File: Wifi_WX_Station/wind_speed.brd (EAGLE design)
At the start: 25.7 x 33.6 mm, 7 parts, among them M1 MRF24WB0MA

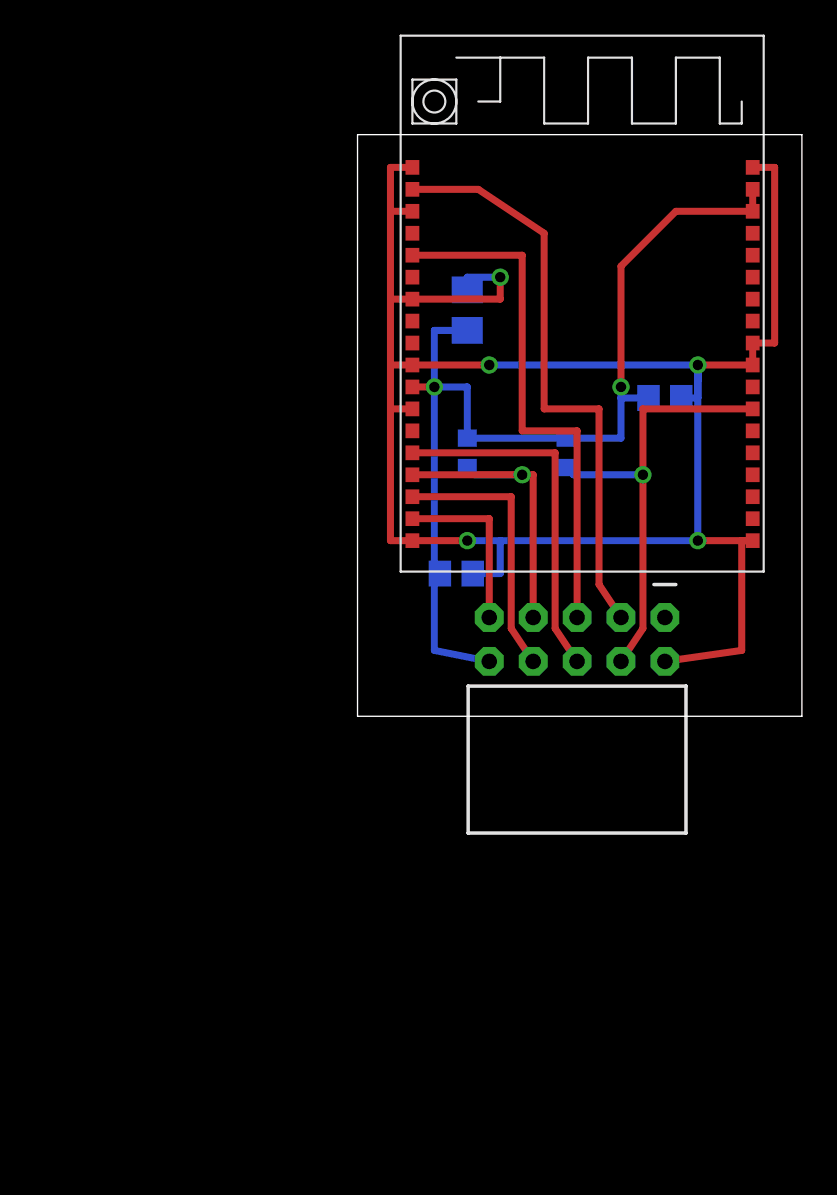
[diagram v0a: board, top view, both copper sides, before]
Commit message: added all the small boards, renamed Wifi module as RH and LH version
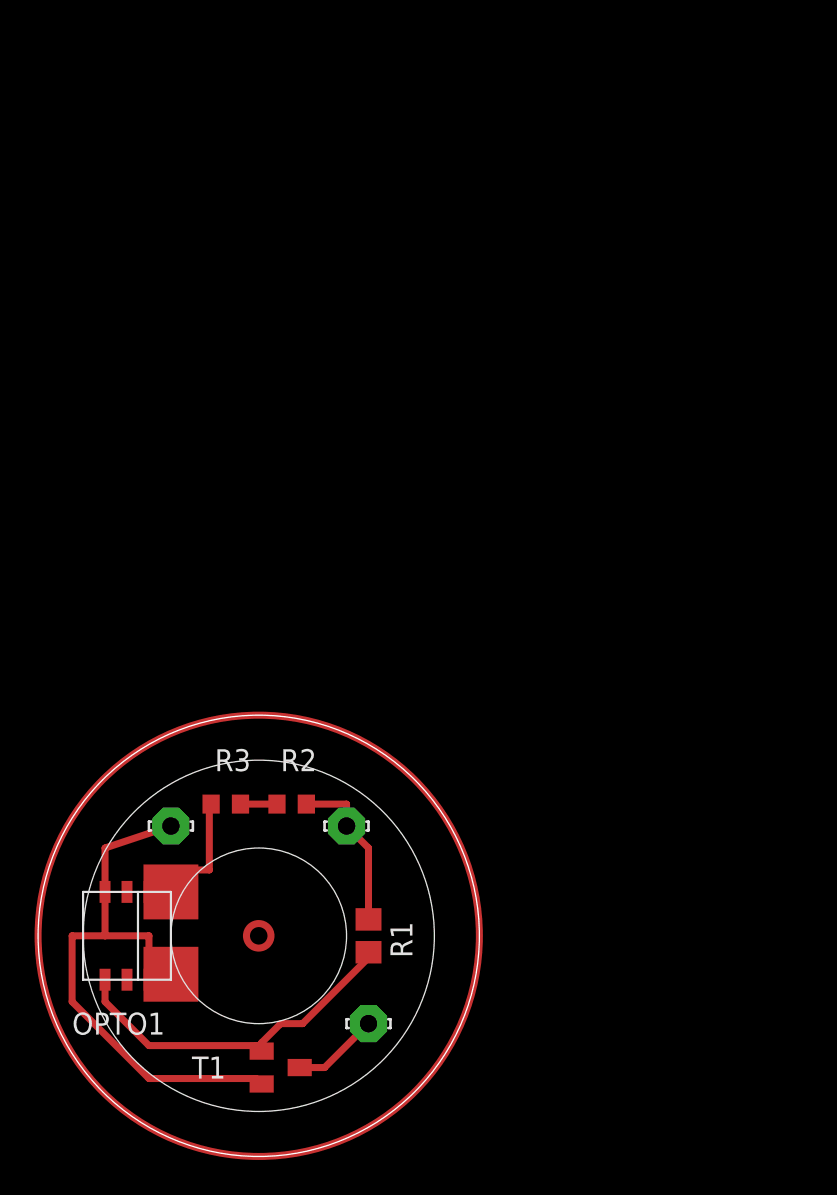
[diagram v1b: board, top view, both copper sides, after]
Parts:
- removed C1, C2: (no value), rcl:C0805
- removed C3: (no value), rcl:R/2012-12R
- removed JP1: M05X2RAF, wifi_WX:2X5-RAF
- removed M1: MRF24WB0MA, 1AA_Stofer:MRF24W
- added +5V, GND, OUT: LSP10, solpad:LSP10
- added OPTO1: OSRAM_SHF9201, 1AA_Stofer:OSRAM-6
- added R3: 120o, rcl:R0603
- added T1: MMBT3904, transistor:SOT23
- R1: value 4.7k -> 10K; device rcl:R0603 -> rcl:R0805
- R2: value 10k -> 120o
- moved R1 28.5 mm to (20.3, 14.0), flipped to the top
- moved R2 25.8 mm to (15.9, 21.6), flipped to the top, turned to 0 degrees
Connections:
- removed net +3V3: C1.1, C2.1, C3.+, JP1.10, M1.16, M1.17, M1.29, R1.2, R2.2
- removed net CS_: JP1.5, M1.23
- removed net GND: C1.2, C2.2, C3.-, JP1.2, M1.1, M1.10, M1.18, M1.19, M1.21, M1.25, M1.28, M1.30, M1.36, M1.9
- removed net HIBER: JP1.3, M1.20
- removed net INT_: JP1.7, M1.33, R1.1
- removed net RESET_: JP1.4, M1.7, R2.1
- removed net SCK: JP1.8, M1.34
- removed net SDI: JP1.9, M1.35
- removed net SDO: JP1.6, M1.32
- new net N$1: OPTO1.P$4, R1.1, T1.1
- new net N$2: GND.MP, OPTO1.P$3, OPTO1.P$6, T1.2
- new net N$3: +5V.MP, R1.2, R2.2
- new net N$4: OUT.MP, T1.3
- new net N$5: OPTO1.P$1, R3.1
- new net N$6: R2.1, R3.2
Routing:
- net GND: track 120.5 -> 0.00 mm, vias 5 -> 0
- net +3V3: track 60.7 -> 0.00 mm, vias 2 -> 0
- net HIBER: track 34.2 -> 0.00 mm
- net N$2: track 0.00 -> 32.8 mm
- net CS_: track 30.5 -> 0.00 mm
- net RESET_: track 26.0 -> 0.00 mm, vias 1 -> 0
- net SDO: track 20.7 -> 0.00 mm
- net N$1: track 0.00 -> 20.5 mm
- net INT_: track 18.6 -> 0.00 mm, vias 1 -> 0
- net SCK: track 15.6 -> 0.00 mm
- net SDI: track 10.2 -> 0.00 mm
- net N$3: track 0.00 -> 9.52 mm
- net N$5: track 0.00 -> 8.67 mm
- net N$4: track 0.00 -> 5.03 mm
- net N$6: track 0.00 -> 2.11 mm
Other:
- board size 25.7 x 33.6 mm -> 25.5 x 25.5 mm
- board text added: "+5V"
- board text added: "GND"
- board text added: "High resolution windspeed encoder"
- board text added: "OUT"
- board text added: "RV-Builders Products 2013"
- board text removed: "0.6000 mm / 23.622 mil"
- board text removed: "0.9000 mm / 35.433 mil"
- board text removed: "1"
- board text removed: "10"
- board text removed: "Date: 12/12/2012 2:51:15 PM"
- board text removed: "Drill legend"
- board text removed: "RV Builders Product 2012"
- board text removed: "Wifi WX-Station"

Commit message: updated BOM with all prices- As Checked in to BATCH PCB
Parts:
- +5V, GND, OUT: value LSP10 -> TPSOL; device solpad:LSP10 -> wifi_WX:TP_SOL
- OPTO1: device 1AA_Stofer:OSRAM-6 -> wifi_WX:OSRAM-6
- R1: device rcl:R0805 -> rcl:R0603
- moved OUT 3.00 mm to (18.7, 6.35)
- moved GND 1.91 mm to (6.99, 20.3)
- moved +5V 1.27 mm to (20.3, 20.3)
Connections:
- net N$2: now also GND.P$1; no longer GND.MP
- net N$3: now also +5V.P$1; no longer +5V.MP
- net N$4: now also OUT.P$1; no longer OUT.MP
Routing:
- net N$4: track 5.03 -> 2.39 mm
- net N$1: track 20.5 -> 22.9 mm
- net N$2: track 32.8 -> 30.6 mm
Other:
- board text added: "High res windspeed encoder"
- board text removed: "High resolution windspeed encoder"

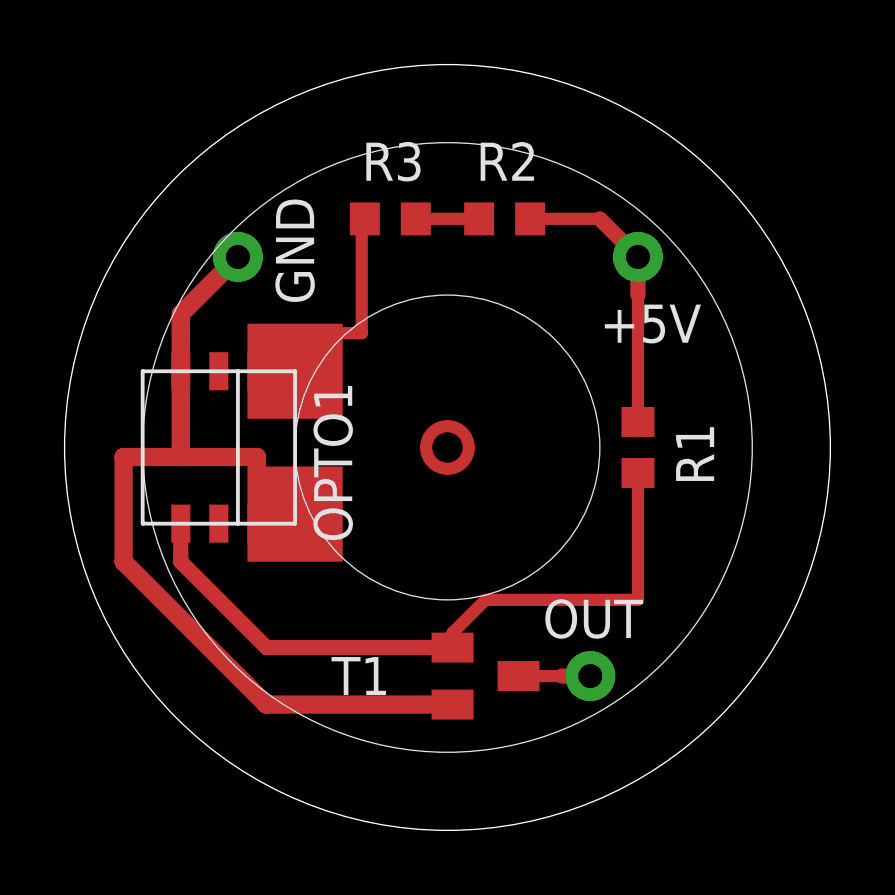
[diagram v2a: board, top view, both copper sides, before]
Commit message: Wind speed board and base station rework to rev HW 1.2
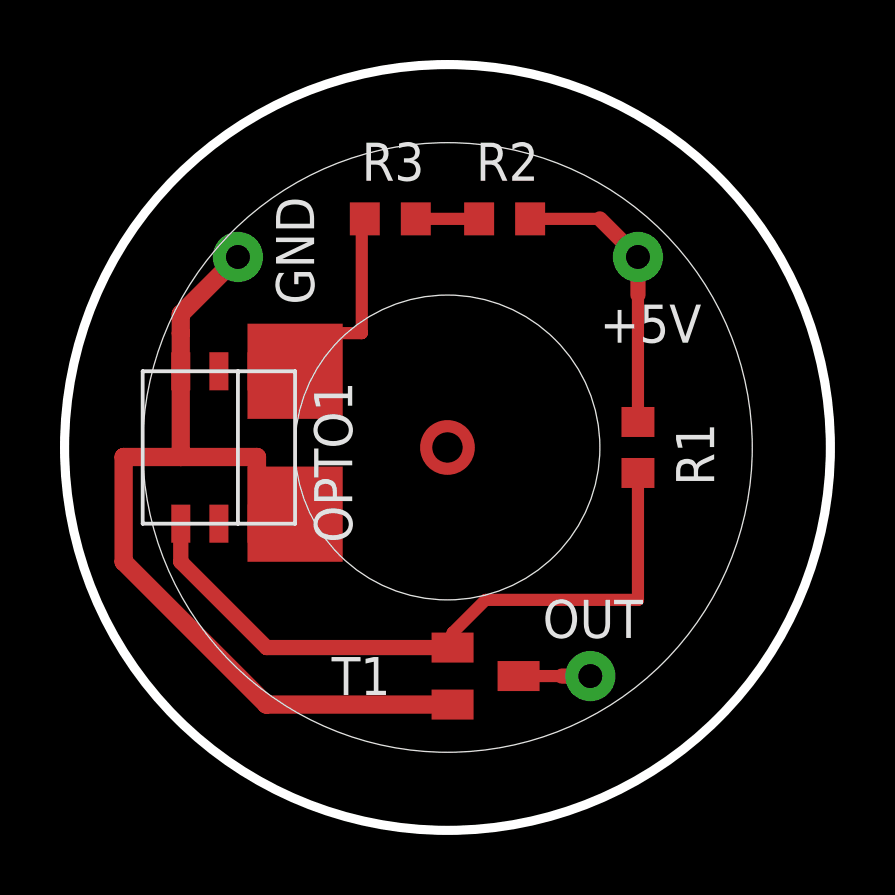
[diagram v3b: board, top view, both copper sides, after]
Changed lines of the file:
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@@
 <grid distance="0.05" unitdist="inch" unit="inch" style="lines" multiple="1" display="yes" altdistance="0.0125" altunitdist="inch" altunit="inch"/>
 <layers>
-<layer number="1" name="Top" color="4" fill="1" visible="no" active="yes"/>
-<layer number="16" name="Bottom" color="1" fill="1" visible="yes" active="yes"/>
+<layer number="1" name="Top" color="4" fill="1" visible="yes" active="yes"/>
+<layer number="16" name="Bottom" color="1" fill="1" visible="no" active="yes"/>
 <layer number="17" name="Pads" color="2" fill="1" visible="yes" active="yes"/>
 <layer number="18" name="Vias" color="2" fill="1" visible="yes" active="yes"/>
-<layer number="19" name="Unrouted" color="6" fill="1" visible="yes" active="yes"/>
+<layer number="19" name="Unrouted" color="6" fill="1" visible="no" active="yes"/>
 <layer number="20" name="Dimension" color="15" fill="1" visible="yes" active="yes"/>
 <layer number="21" name="tPlace" color="7" fill="1" visible="no" active="yes"/>
-<layer number="22" name="bPlace" color="7" fill="1" visible="yes" active="yes"/>
+<layer number="22" name="bPlace" color="7" fill="1" visible="no" active="yes"/>
 <layer number="23" name="tOrigins" color="15" fill="1" visible="no" active="yes"/>
-<layer number="24" name="bOrigins" color="15" fill="1" visible="yes" active="yes"/>
+<layer number="24" name="bOrigins" color="15" fill="1" visible="no" active="yes"/>
 <layer number="25" name="tNames" color="7" fill="1" visible="no" active="yes"/>
-<layer number="26" name="bNames" color="7" fill="1" visible="yes" active="yes"/>
+<layer number="26" name="bNames" color="7" fill="1" visible="no" active="yes"/>
 <layer number="27" name="tValues" color="7" fill="1" visible="no" active="yes"/>
-<layer number="28" name="bValues" color="7" fill="1" visible="yes" active="yes"/>
+<layer number="28" name="bValues" color="7" fill="1" visible="no" active="yes"/>
 <layer number="29" name="tStop" color="7" fill="3" visible="no" active="yes"/>
 <layer number="30" name="bStop" color="7" fill="6" visible="no" active="yes"/>
@@
 <layer number="43" name="vRestrict" color="2" fill="10" visible="no" active="yes"/>
 <layer number="44" name="Drills" color="7" fill="1" visible="no" active="yes"/>
-<layer number="45" name="Holes" color="7" fill="1" visible="yes" active="yes"/>
+<layer number="45" name="Holes" color="7" fill="1" visible="no" active="yes"/>
 <layer number="46" name="Milling" color="3" fill="1" visible="no" active="yes"/>
 <layer number="47" name="Measures" color="7" fill="1" visible="no" active="yes"/>
@@
 <layer number="50" name="dxf" color="7" fill="1" visible="no" active="no"/>
 <layer number="51" name="tDocu" color="7" fill="1" visible="no" active="yes"/>
-<layer number="52" name="bDocu" color="7" fill="1" visible="yes" active="yes"/>
+<layer number="52" name="bDocu" color="7" fill="1" visible="no" active="yes"/>
 <layer number="53" name="tGND_GNDA" color="7" fill="9" visible="no" active="no"/>
 <layer number="54" name="bGND_GNDA" color="1" fill="9" visible="no" active="no"/>
@@
 <board>
 <plain>
-<circle x="13.97" y="13.97" radius="12.763340625" width="0.0254" layer="20"/>
+<circle x="13.97" y="13.97" radius="12.763340625" width="0.3048" layer="20"/>
 <circle x="13.97" y="13.97" radius="10.16" width="0.0254" layer="21"/>
 <circle x="13.97" y="13.97" radius="5.08" width="0.0254" layer="21"/>

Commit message: Revision B.1
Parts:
- added R4: 1K, rcl:R0603
- added R5: 330, rcl:R0603
- moved OUT 2.22 mm to (16.5, 6.35)
- moved T1 1.90 mm to (13.3, 6.35)
- moved GND 0.45 mm to (7.30, 20.0)
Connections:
- net N$3: now also R4.2
- net N$4: now also R4.1, R5.1
- net N$6: now also R5.2
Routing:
- net N$4: track 2.39 -> 20.6 mm
- net N$6: track 2.11 -> 14.1 mm, vias 0 -> 1
- net N$3: track 9.62 -> 13.9 mm
- net N$2: track 30.6 -> 27.3 mm
- net N$1: track 22.9 -> 21.3 mm
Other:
- board size 25.5 x 25.5 mm -> 25.5 x 25.4 mm
- board text added: "AN27 Revision B.1"

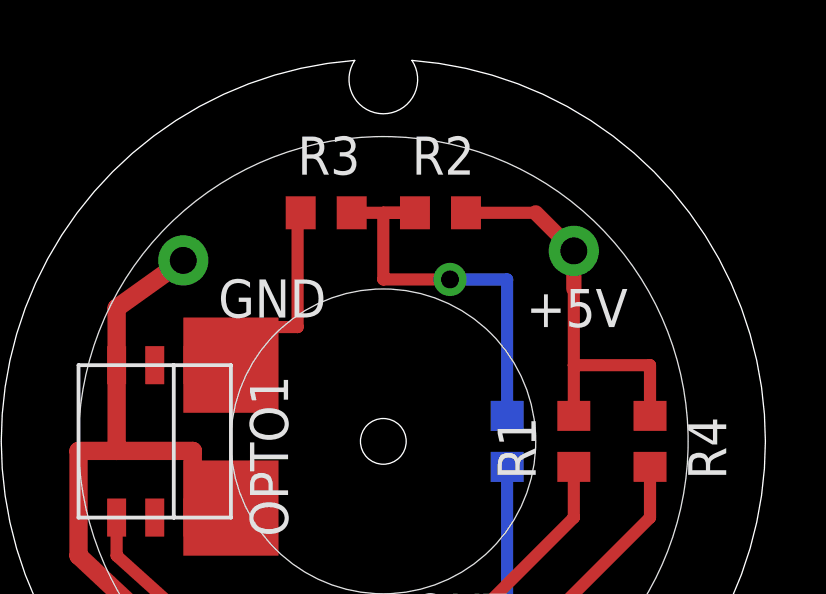
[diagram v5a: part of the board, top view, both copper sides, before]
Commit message: added SILabs Hygrometer board Added frames to the schematics
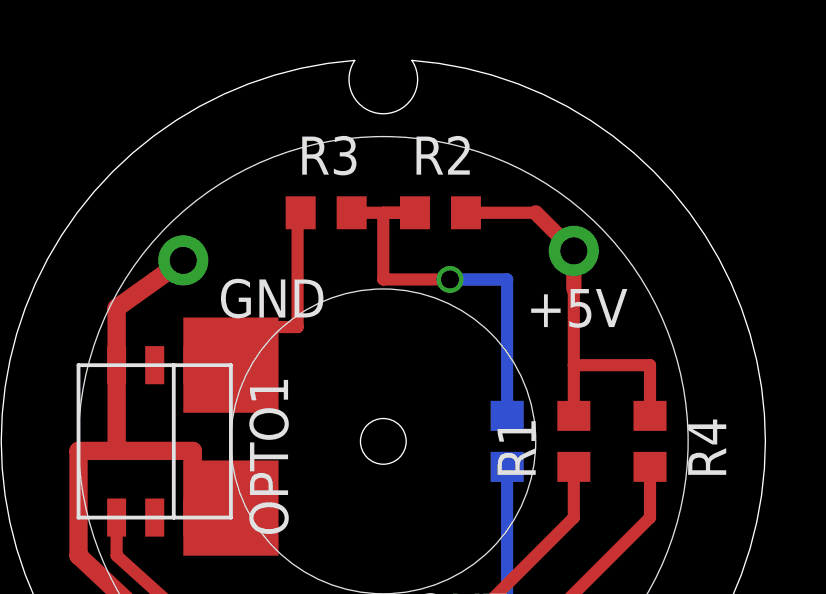
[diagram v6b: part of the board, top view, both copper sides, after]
